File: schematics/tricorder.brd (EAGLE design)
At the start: 90.2 x 73.7 mm, 77 parts, among them IC1 EADOGM128, Q1 MOSFET-NCHANNELBSS138, U1 V_REG_LDOSMD, U2 CY8C5XXX, U3 M05X2-0.05-SMD, U7 MICROUSB

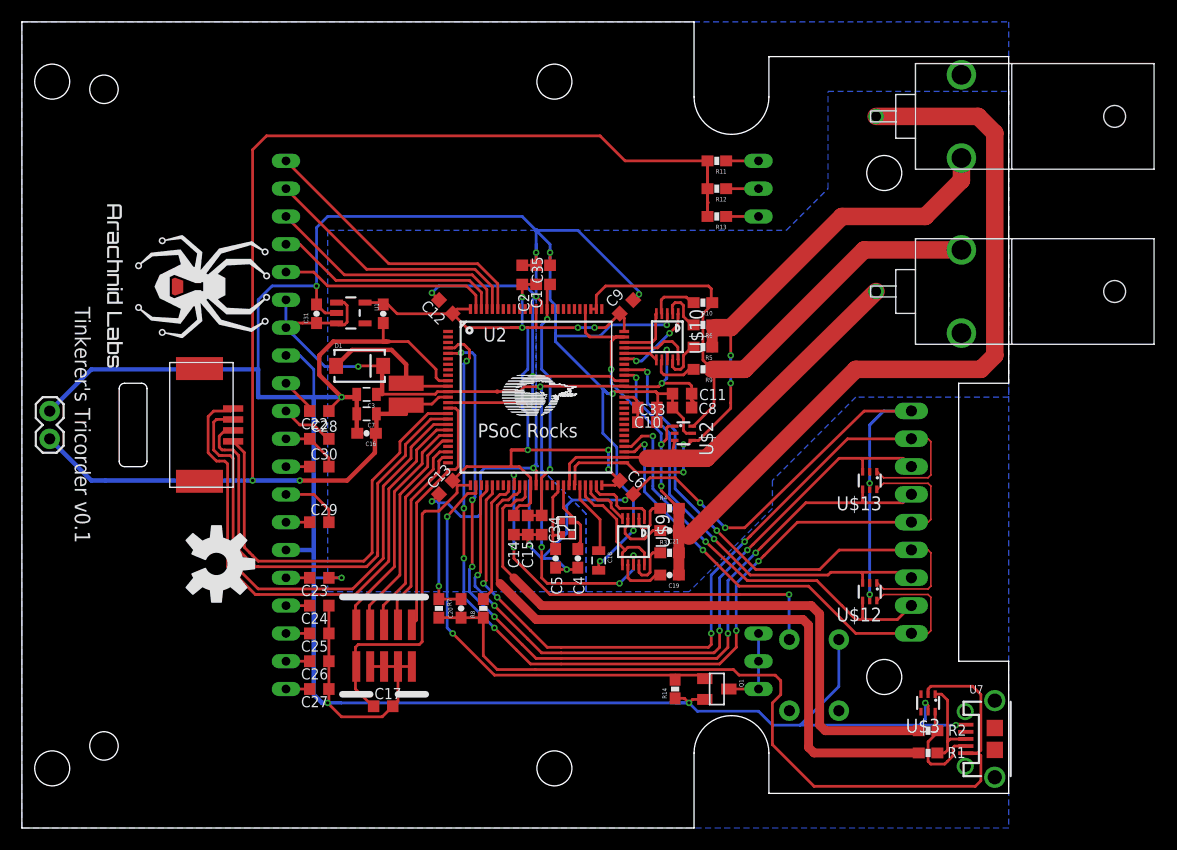
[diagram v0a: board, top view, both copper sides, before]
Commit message: Tweaked position of BNCs
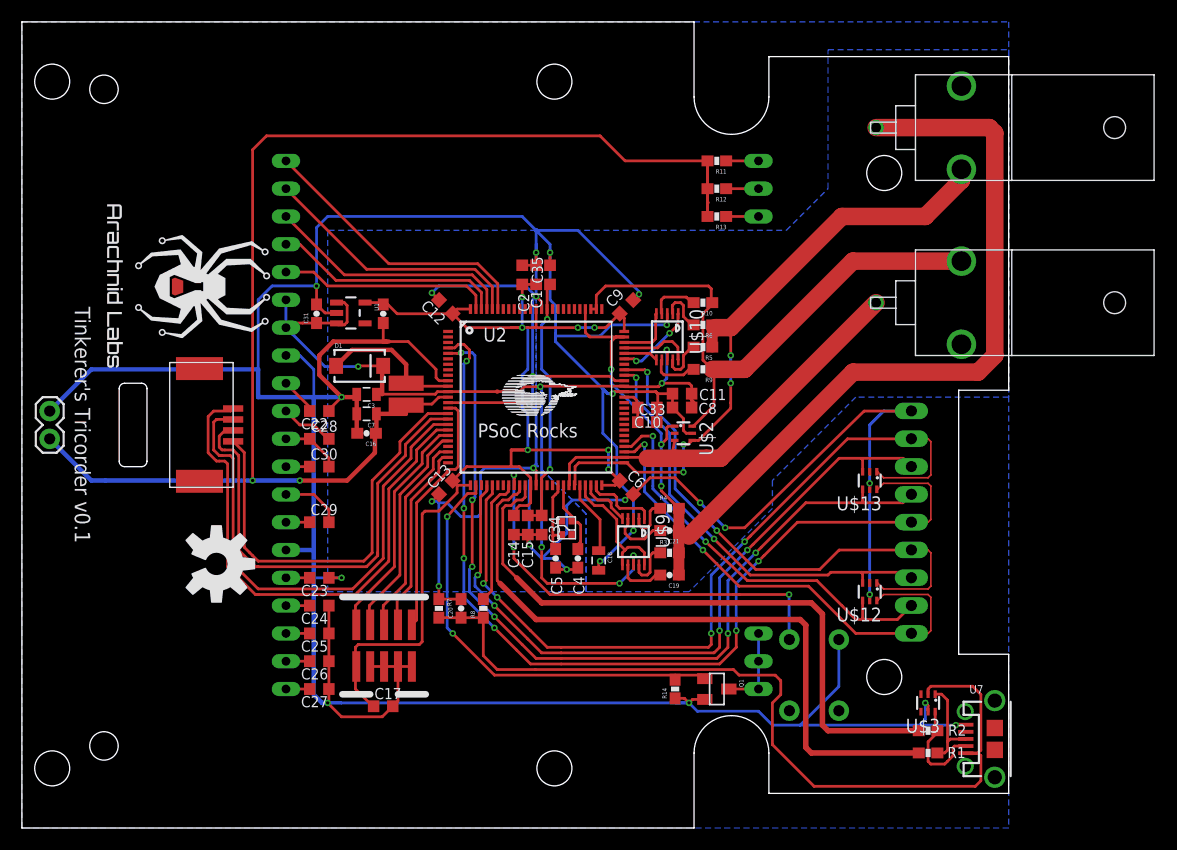
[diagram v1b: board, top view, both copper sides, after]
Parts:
- moved U$11 1.02 mm to (85.9, 48.0)
- moved U$4 1.02 mm to (85.9, 64.0)
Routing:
- net BNC1_TIP: track 60.3 -> 59.3 mm
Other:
- outline, holes or cut-outs redrawn
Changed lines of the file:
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@@
 <grid distance="1.27" unitdist="mm" unit="mm" style="lines" multiple="1" display="yes" altdistance="10" altunitdist="mil" altunit="mil"/>
 <layers>
-<layer number="1" name="Top" color="4" fill="1" visible="no" active="yes"/>
-<layer number="16" name="Bottom" color="1" fill="1" visible="no" active="yes"/>
+<layer number="1" name="Top" color="4" fill="1" visible="yes" active="yes"/>
+<layer number="16" name="Bottom" color="1" fill="1" visible="yes" active="yes"/>
 <layer number="17" name="Pads" color="2" fill="1" visible="yes" active="yes"/>
 <layer number="18" name="Vias" color="2" fill="1" visible="yes" active="yes"/>
@@
 <hole x="48.66" y="5.45" drill="3.2"/>
 <hole x="2.77" y="68.2" drill="3.2"/>
-<wire x1="85.598" y1="40.64" x2="85.598" y2="15.24" width="0" layer="20"/>
-<wire x1="85.598" y1="40.64" x2="90.17" y2="40.64" width="0" layer="20"/>
-<wire x1="85.598" y1="15.24" x2="90.17" y2="15.24" width="0" layer="20"/>
-<wire x1="90.17" y1="70.485" x2="90.17" y2="40.64" width="0" layer="20"/>
-<wire x1="90.17" y1="15.24" x2="90.17" y2="3.165" width="0" layer="20"/>
+<wire x1="85.598" y1="40.005" x2="85.598" y2="15.875" width="0" layer="20"/>
+<wire x1="85.598" y1="40.005" x2="90.17" y2="40.005" width="0" layer="20"/>
+<wire x1="85.598" y1="15.875" x2="90.17" y2="15.875" width="0" layer="20"/>
+<wire x1="90.17" y1="70.485" x2="90.17" y2="40.005" width="0" layer="20"/>
+<wire x1="90.17" y1="15.875" x2="90.17" y2="3.165" width="0" layer="20"/>
 <circle x="78.8" y="59.85" radius="2.5" width="0" layer="39"/>
 <circle x="78.8" y="13.8" radius="2.5" width="0" layer="39"/>
@@
 <attribute name="NAME" x="58.928" y="11.811" size="0.4064" layer="25" font="vector" rot="R90"/>
 </element>
-<element name="U$4" library="nickparts" package="BNC_RA" value="BNC" x="85.852" y="65.024" smashed="yes" rot="R90"/>
-<element name="U$11" library="nickparts" package="BNC_RA" value="BNC" x="85.852" y="49.024" smashed="yes" rot="R90"/>
+<element name="U$4" library="nickparts" package="BNC_RA" value="BNC" x="85.852" y="64" smashed="yes" rot="R90"/>
+<element name="U$11" library="nickparts" package="BNC_RA" value="BNC" x="85.852" y="48" smashed="yes" rot="R90"/>
 <element name="C33" library="resistor" package="C0603K" value="0.1u" x="57.15" y="37.084" smashed="yes">
 <attribute name="NAME" x="56.35" y="37.734" size="1.016" layer="25"/>
@@
 <contactref element="R1" pad="1"/>
 <contactref element="U2" pad="35"/>
-<wire x1="46.99" y1="19.05" x2="43.688" y2="22.352" width="0.8128" layer="1"/>
-<wire x1="46.99" y1="19.05" x2="71.374" y2="19.05" width="0.8128" layer="1"/>
-<wire x1="71.374" y1="19.05" x2="71.882" y2="18.542" width="0.8128" layer="1"/>
-<wire x1="71.882" y1="18.542" x2="71.882" y2="7.366" width="0.8128" layer="1"/>
-<wire x1="71.882" y1="7.366" x2="72.39" y2="6.858" width="0.8128" layer="1"/>
-<wire x1="72.39" y1="6.858" x2="81.954" y2="6.858" width="0.8128" layer="1"/>
+<wire x1="46.99" y1="19.05" x2="43.688" y2="22.352" width="0.508" layer="1"/>
+<wire x1="46.99" y1="19.05" x2="71.12" y2="19.05" width="0.508" layer="1"/>
+<wire x1="71.12" y1="19.05" x2="71.628" y2="18.542" width="0.508" layer="1"/>
+<wire x1="71.628" y1="18.542" x2="71.628" y2="7.366" width="0.508" layer="1"/>
+<wire x1="71.628" y1="7.366" x2="72.136" y2="6.858" width="0.508" layer="1"/>
+<wire x1="72.136" y1="6.858" x2="81.954" y2="6.858" width="0.508" layer="1"/>
 <wire x1="45.49" y1="31.32" x2="45.49" y2="30.758" width="0.254" layer="1"/>
 <wire x1="45.49" y1="30.758" x2="45.212" y2="30.48" width="0.254" layer="1"/>
@@
 <contactref element="R2" pad="1"/>
 <contactref element="U2" pad="36"/>
-<wire x1="47.498" y1="20.32" x2="44.958" y2="22.86" width="0.8128" layer="1"/>
-<wire x1="47.498" y1="20.32" x2="72.136" y2="20.32" width="0.8128" layer="1"/>
-<wire x1="72.136" y1="20.32" x2="72.898" y2="19.558" width="0.8128" layer="1"/>
-<wire x1="72.898" y1="19.558" x2="72.898" y2="9.398" width="0.8128" layer="1"/>
-<wire x1="72.898" y1="9.398" x2="73.406" y2="8.89" width="0.8128" layer="1"/>
-<wire x1="73.406" y1="8.89" x2="81.954" y2="8.89" width="0.8128" layer="1"/>
+<wire x1="47.498" y1="20.574" x2="45.212" y2="22.86" width="0.508" layer="1"/>
+<wire x1="47.498" y1="20.574" x2="72.136" y2="20.574" width="0.508" layer="1"/>
+<wire x1="72.136" y1="20.574" x2="73.152" y2="19.558" width="0.508" layer="1"/>
+<wire x1="73.152" y1="19.558" x2="73.152" y2="9.398" width="0.508" layer="1"/>
+<wire x1="73.152" y1="9.398" x2="73.66" y2="8.89" width="0.508" layer="1"/>
+<wire x1="73.66" y1="8.89" x2="81.954" y2="8.89" width="0.508" layer="1"/>
 <wire x1="45.99" y1="31.32" x2="45.99" y2="30.242" width="0.254" layer="1"/>
 <wire x1="45.99" y1="30.242" x2="45.72" y2="29.972" width="0.254" layer="1"/>
@@
 <wire x1="44.704" y1="29.464" x2="44.196" y2="29.464" width="0.254" layer="1"/>
 <wire x1="44.196" y1="29.464" x2="43.942" y2="29.21" width="0.254" layer="1"/>
-<wire x1="43.942" y1="29.21" x2="43.942" y2="23.876" width="0.254" layer="1"/>
-<wire x1="43.942" y1="23.876" x2="44.958" y2="22.86" width="0.254" layer="1"/>
+<wire x1="43.942" y1="29.21" x2="43.942" y2="24.13" width="0.254" layer="1"/>
+<wire x1="43.942" y1="24.13" x2="45.212" y2="22.86" width="0.254" layer="1"/>
 </signal>
 <signal name="CLKI">
@@
 <vertex x="69.85" y="54.61"/>
 <vertex x="73.66" y="58.42"/>
-<vertex x="73.66" y="67.31"/>
-<vertex x="90.17" y="67.31"/>
+<vertex x="73.66" y="71.12"/>
+<vertex x="90.17" y="71.12"/>
 <vertex x="90.17" y="39.37"/>
 <vertex x="76.2" y="39.37"/>
@@
 <contactref element="U$4" pad="SHIELD_2" route="any" routetag="GND"/>
 <contactref element="U$4" pad="SHIELD_1" route="any" routetag="GND"/>
-<wire x1="85.852" y1="61.224" x2="85.852" y2="59.182" width="1.6" layer="1"/>
+<wire x1="85.852" y1="60.2" x2="85.852" y2="59.182" width="1.6" layer="1"/>
 <wire x1="85.852" y1="59.182" x2="82.55" y2="55.88" width="1.6" layer="1"/>
 <wire x1="82.55" y1="55.88" x2="74.93" y2="55.88" width="1.6" layer="1"/>
@@
 <contactref element="C19" pad="1"/>
 <contactref element="U$4" pad="TIP"/>
-<wire x1="78.052" y1="65.024" x2="87.376" y2="65.024" width="1.6" layer="1"/>
-<wire x1="87.376" y1="65.024" x2="88.9" y2="63.5" width="1.6" layer="1"/>
 <wire x1="88.9" y1="63.5" x2="88.9" y2="43.18" width="1.6" layer="1"/>
-<wire x1="88.9" y1="43.18" x2="87.63" y2="41.91" width="1.6" layer="1"/>
-<wire x1="87.63" y1="41.91" x2="76.2" y2="41.91" width="1.6" layer="1"/>
-<wire x1="76.2" y1="41.91" x2="60.96" y2="26.67" width="1.6" layer="1"/>
+<wire x1="88.9" y1="43.18" x2="87.376" y2="41.656" width="1.6" layer="1"/>
+<wire x1="87.376" y1="41.656" x2="75.946" y2="41.656" width="1.6" layer="1"/>
+<wire x1="75.946" y1="41.656" x2="60.96" y2="26.67" width="1.6" layer="1"/>
 <wire x1="60.032" y1="29.21" x2="60.032" y2="27.178" width="1" layer="1"/>
 <wire x1="60.032" y1="27.178" x2="60.032" y2="26.67" width="1" layer="1"/>
@@
 <wire x1="53.848" y1="40.64" x2="58.42" y2="36.068" width="0.254" layer="16"/>
 <wire x1="58.42" y1="36.068" x2="58.42" y2="35.052" width="0.254" layer="16"/>
+<wire x1="78.052" y1="64" x2="88.4" y2="64" width="1.6" layer="1"/>
+<wire x1="88.4" y1="64" x2="88.9" y2="63.5" width="1.6" layer="1"/>
 </signal>
 <signal name="BNC2_TIP">
@@
 <wire x1="57.15" y1="33.782" x2="59.69" y2="33.782" width="1.6" layer="1"/>
 <wire x1="59.69" y1="33.782" x2="62.556" y2="33.782" width="1.6" layer="1"/>
-<wire x1="62.556" y1="33.782" x2="78.052" y2="49.024" width="1.6" layer="1"/>
 <contactref element="U$2" pad="3"/>
 <wire x1="59.652" y1="35.418" x2="59.398" y2="34.074" width="0.254" layer="1"/>
 <wire x1="59.398" y1="34.074" x2="59.69" y2="33.782" width="0.254" layer="1"/>
+<wire x1="62.556" y1="33.782" x2="63.834" y2="33.782" width="1.6" layer="1"/>
+<wire x1="63.834" y1="33.782" x2="78.052" y2="48" width="1.6" layer="1"/>
 </signal>
 <signal name="BNC2_SHIELD">
@@
 <contactref element="U$11" pad="SHIELD_2" route="any" routetag="GND"/>
 <contactref element="U$11" pad="SHIELD_1" route="any" routetag="GND"/>
-<wire x1="85.852" y1="52.824" x2="76.954" y2="52.824" width="1.6" layer="1"/>
-<wire x1="76.954" y1="52.824" x2="66.04" y2="41.91" width="1.6" layer="1"/>
 <wire x1="66.04" y1="41.91" x2="63.08" y2="41.91" width="1.6" layer="1"/>
 <wire x1="61.252" y1="36.718" x2="61.356" y2="36.718" width="0.254" layer="1"/>
@@
 <wire x1="63.246" y1="38.608" x2="63.246" y2="41.744" width="0.254" layer="1"/>
 <wire x1="63.246" y1="41.744" x2="63.08" y2="41.91" width="0.254" layer="1"/>
+<wire x1="85.852" y1="51.8" x2="75.93" y2="51.8" width="1.6" layer="1"/>
+<wire x1="75.93" y1="51.8" x2="66.04" y2="41.91" width="1.6" layer="1"/>
 </signal>
 <signal name="BNC1_TIP_FB">
@@
 <wire x1="40.386" y1="24.638" x2="40.386" y2="21.082" width="0.254" layer="16"/>
 <wire x1="40.386" y1="21.082" x2="43.18" y2="18.288" width="0.254" layer="16"/>
-<via x="43.18" y="18.288" extent="1-16" drill="0.3"/>
-<wire x1="43.18" y1="18.288" x2="45.212" y2="16.256" width="0.254" layer="1"/>
 <wire x1="40.64" y1="42.672" x2="40.386" y2="42.418" width="0.254" layer="16"/>
 <wire x1="40.386" y1="42.418" x2="40.386" y2="29.21" width="0.254" layer="16"/>
@@
 <wire x1="70.866" y1="27.94" x2="81.27" y2="27.94" width="0.254" layer="1"/>
 <wire x1="81.27" y1="27.94" x2="81.28" y2="27.95" width="0.254" layer="1"/>
+<via x="43.18" y="18.288" extent="1-16" drill="0.3"/>
+<wire x1="43.18" y1="18.288" x2="45.212" y2="16.256" width="0.254" layer="1"/>
 </signal>
 <signal name="D3">

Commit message: Design and layout modifications: onboard BNC, dedicated backlight controller
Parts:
- removed Q1: MOSFET-NCHANNELBSS138, SparkFun-DiscreteSemi:SOT23
- removed R11, R12, R13: 22, SparkFun-Passives:0603-RES
- removed R14: 10k, SparkFun-Passives:0603-RES
- added C36: 1u, resistor:C0603K
- added U$16: CAT4003B, nickparts:SOT23-6
- added U$17: (no value), nickparts:STENCIL8_FIDUCIAL
- moved U7 0.28 mm to (88.9, 8.42)
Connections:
- removed net N$24: IC1.18, IC1.19, IC1.20, Q1.3
- net GND: now also C36.1, U$16.2; no longer Q1.2, R14.1
- net LED_BL: now also U$16.1; no longer Q1.1, R14.2
- net N$22: now also IC1.18, U$16.6; no longer IC1.1, R11.1
- net N$23: now also IC1.19, U$16.5; no longer IC1.2, R12.1
- net N$25: now also IC1.20, U$16.4; no longer IC1.3, R13.1
- net V+: now also C36.2, IC1.1, IC1.2, IC1.3, U$16.3; no longer R11.2, R12.2, R13.2
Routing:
- net V+: track 133.9 -> 204.7 mm, vias 2 -> 3
- net N$24: track 7.79 -> 0.00 mm
- net N$22: track 2.96 -> 5.23 mm
- net N$FOO: track 78.7 -> 76.6 mm
- net GND: track 244.7 -> 246.2 mm
- net N$23: track 2.96 -> 4.01 mm
- net D5: track 78.4 -> 78.5 mm, vias 6 -> 4
- net D7: track 72.7 -> 72.8 mm, vias 4 -> 2
- net D4: vias 6 -> 4
- net D6: vias 4 -> 2

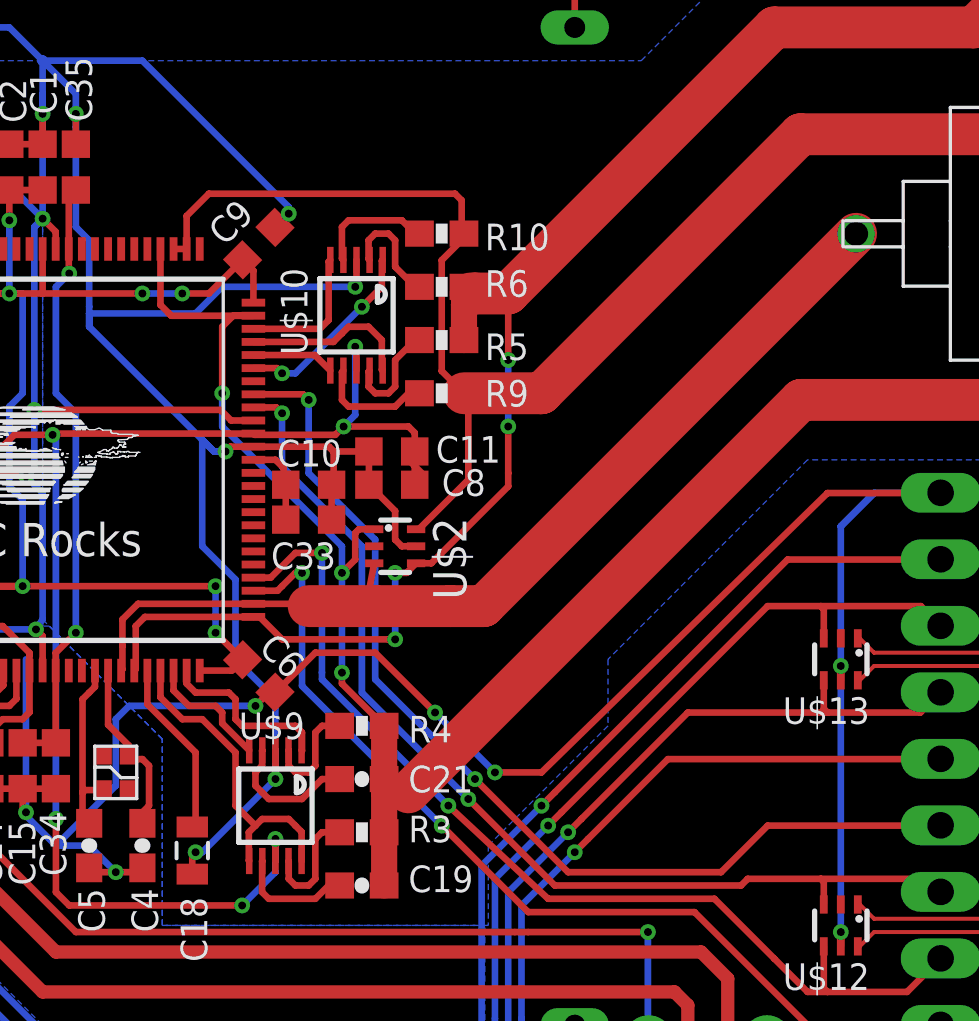
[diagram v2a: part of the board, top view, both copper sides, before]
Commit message: Modified tricorder code so it compiles in a basic fashion; TRM and schematic fixes.
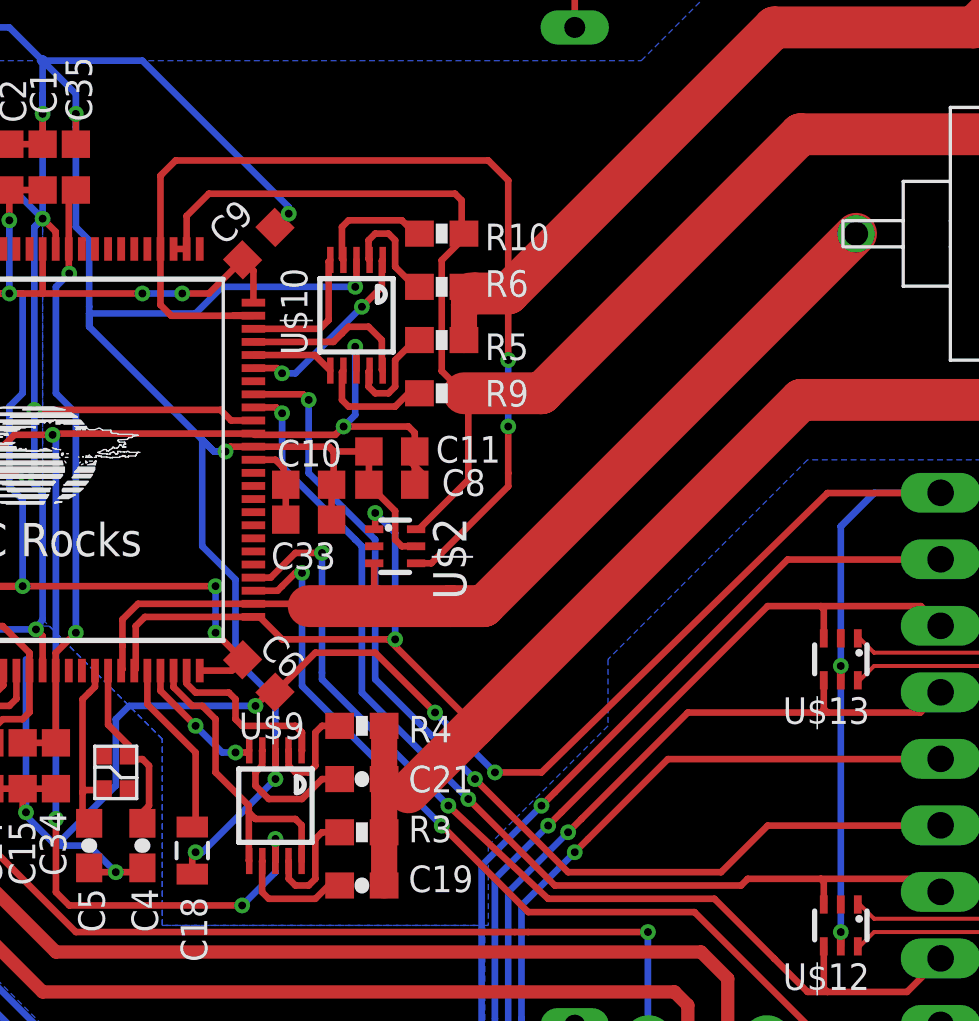
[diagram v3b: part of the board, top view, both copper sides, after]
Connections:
- net BNC1_SHIELD: now also R5.1, R6.1, U$2.4, U$4.SHIELD_1, U$4.SHIELD_2; no longer C19.1, C21.1, R3.2, R4.2, U$2.1, U$4.TIP
- net BNC1_TIP: now also C19.1, C21.1, R3.2, R4.2, U$2.1, U$4.TIP; no longer R5.1, R6.1, U$2.4, U$4.SHIELD_1, U$4.SHIELD_2
- net BNC1_TIP_FB: now also U2.48; no longer U2.47
- net BNC1_TIP_LPF: now also U2.47; no longer U2.48
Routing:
- net BNC1_TIP: track 59.3 -> 95.8 mm, vias 4 -> 2
- net BNC1_SHIELD: track 100.7 -> 73.1 mm, vias 3 -> 2
- net BNC1_TIP_LPF: track 4.84 -> 5.17 mm, vias 0 -> 2
